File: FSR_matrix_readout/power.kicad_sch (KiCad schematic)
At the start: 8 parts, among them U25 TPS7A2033PDBVR, U26 LM321

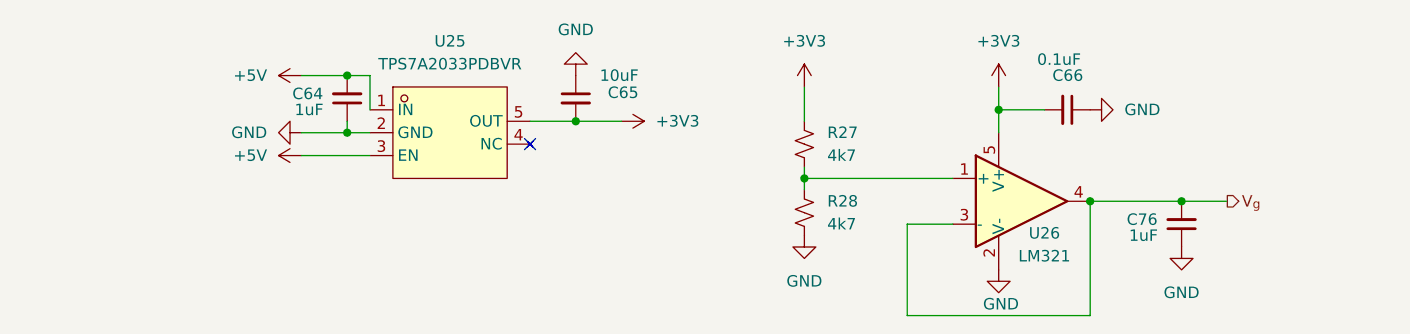
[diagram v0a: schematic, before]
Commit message: add dual feedback for Vg opamp
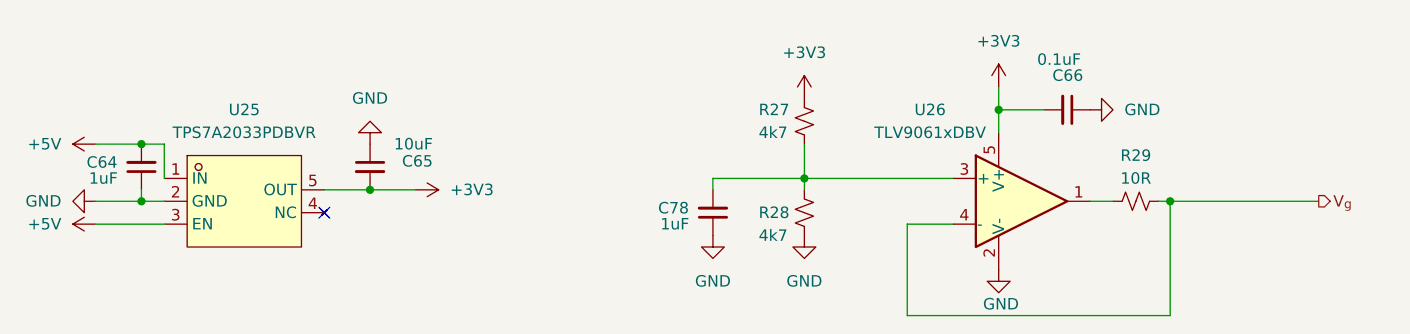
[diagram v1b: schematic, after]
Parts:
- removed C76: 1uF, symbol Device:C_Small
- removed U26: LM321, Package_TO_SOT_SMD:SOT-23-5, symbol Amplifier_Operational:LM321
- added C78: 1uF, symbol Device:C_Small
- added R29: 10R, symbol Device:R_Small_US
- added U26: TLV9061xDBV, Package_TO_SOT_SMD:SOT-23-5, symbol Amplifier_Operational:TLV9061xDBV
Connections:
- net +3V3: now also U26.5 (V+)
- net GND: now also C78.1, U26.2 (V-)
- net V_{g}: now also R29.1, U26.4 (-)
- net at R27.2, R28.1: now also C78.2, U26.3 (+)
- new net: R29.2, U26.1
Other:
- moved on the sheet: C64, C65, R27, U25

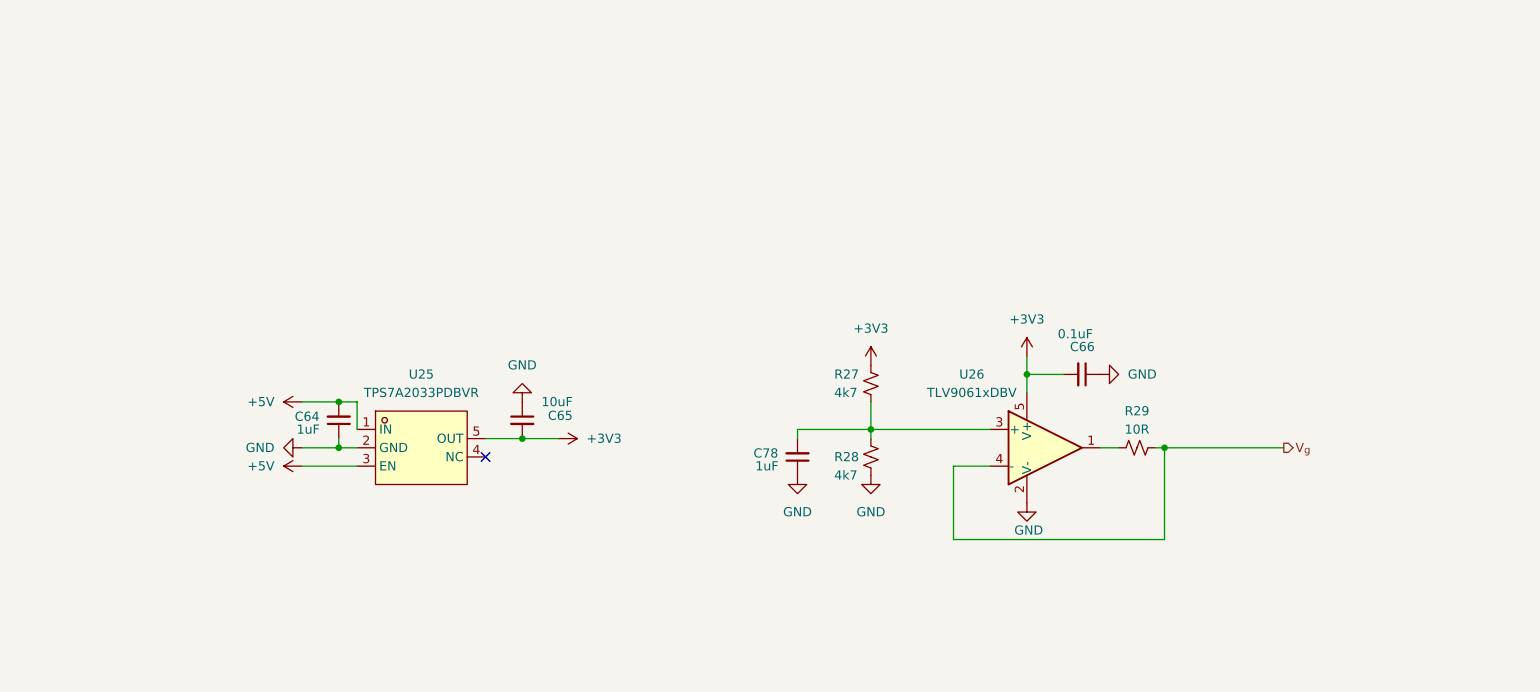
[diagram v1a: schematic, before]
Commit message: added some test points
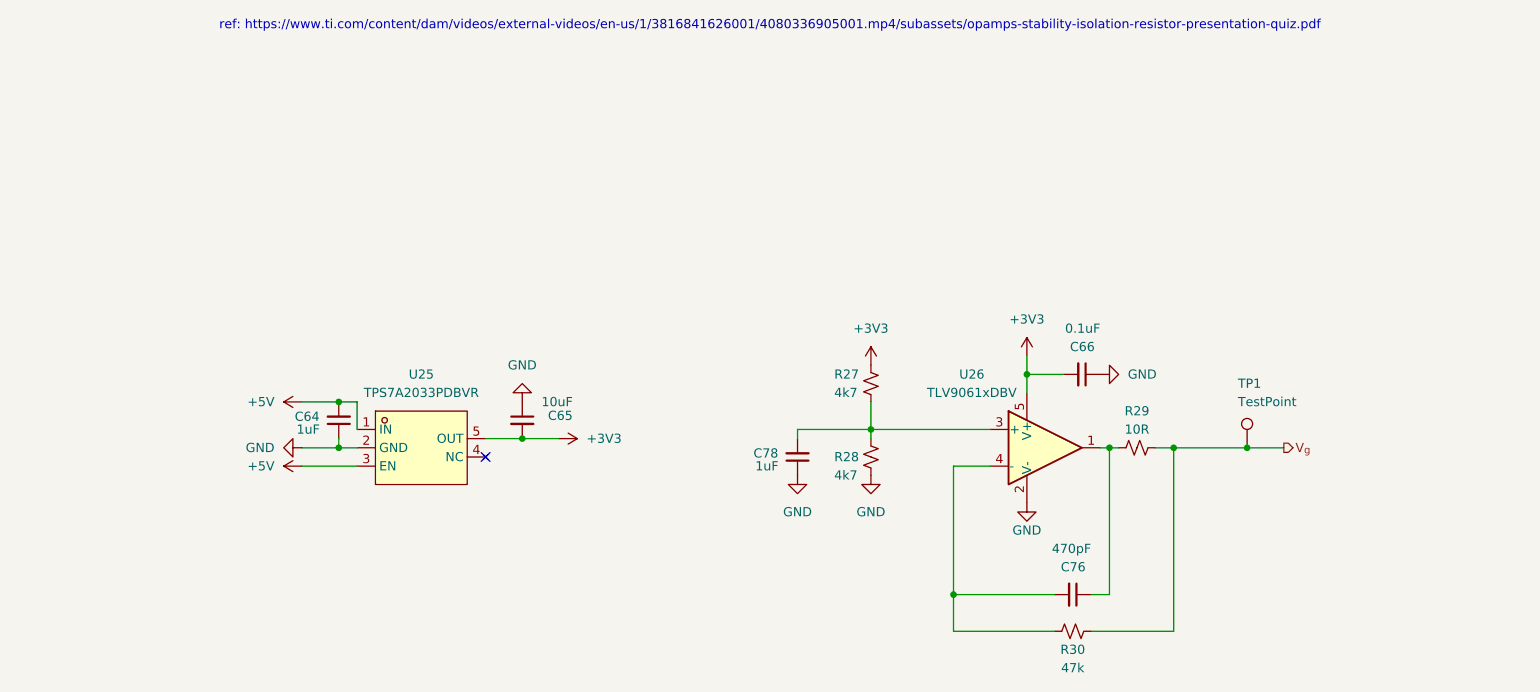
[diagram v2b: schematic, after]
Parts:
- added C76: 470pF, symbol Device:C_Small
- added R30: 47k, symbol Device:R_Small_US
- added TP1: TestPoint, symbol Connector:TestPoint
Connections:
- net V_{g}: now also R30.2, TP1.1; no longer U26.4 (-)
- net at R29.2, U26.1: now also C76.1
- new net: C76.2, R30.1, U26.4 (-)
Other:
- note added: "ref: https://www.ti.com/content/dam/videos/external-videos/en-us/1/3816841626001/4080336905001.mp4/subassets/opamps-stability-isolation-resistor-presentation-quiz.pdf"
